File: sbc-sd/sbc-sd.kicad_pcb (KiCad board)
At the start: 4 copper layers, 55.9 x 25.4 mm, 21 parts, among them J1 SIO-Header, J2 RP2040-Zero-lhs, J3 RP2040-Zero-rhs, J4 RP2040-Zero-bottom, J5 104031-0811, U1 TXU0304, U2 LD39015M33R

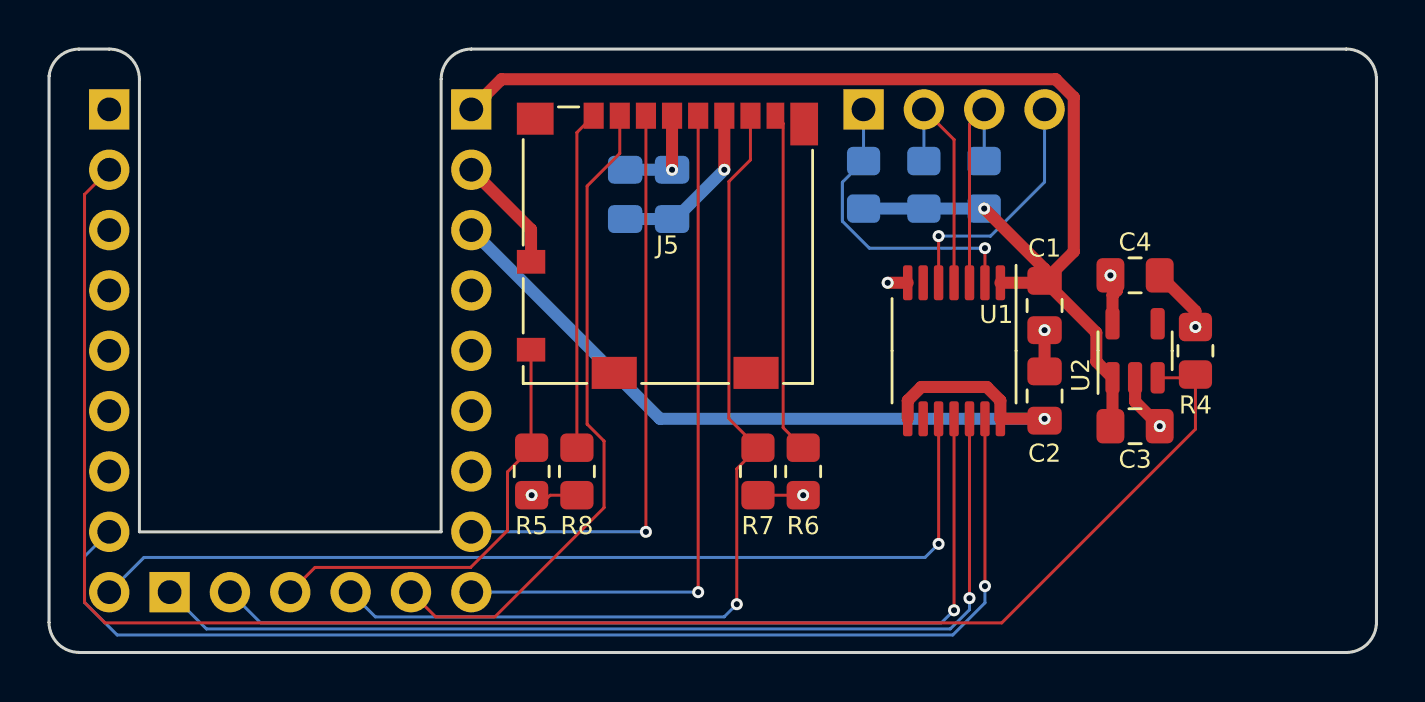
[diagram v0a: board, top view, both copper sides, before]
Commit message: SD card adapter v1.2
- Move SD card connector closer to the edge of the board
- Pullup SD detect signal to non-switched 5V
- Eliminate SD DO pullup
- Move LDO closer to SD
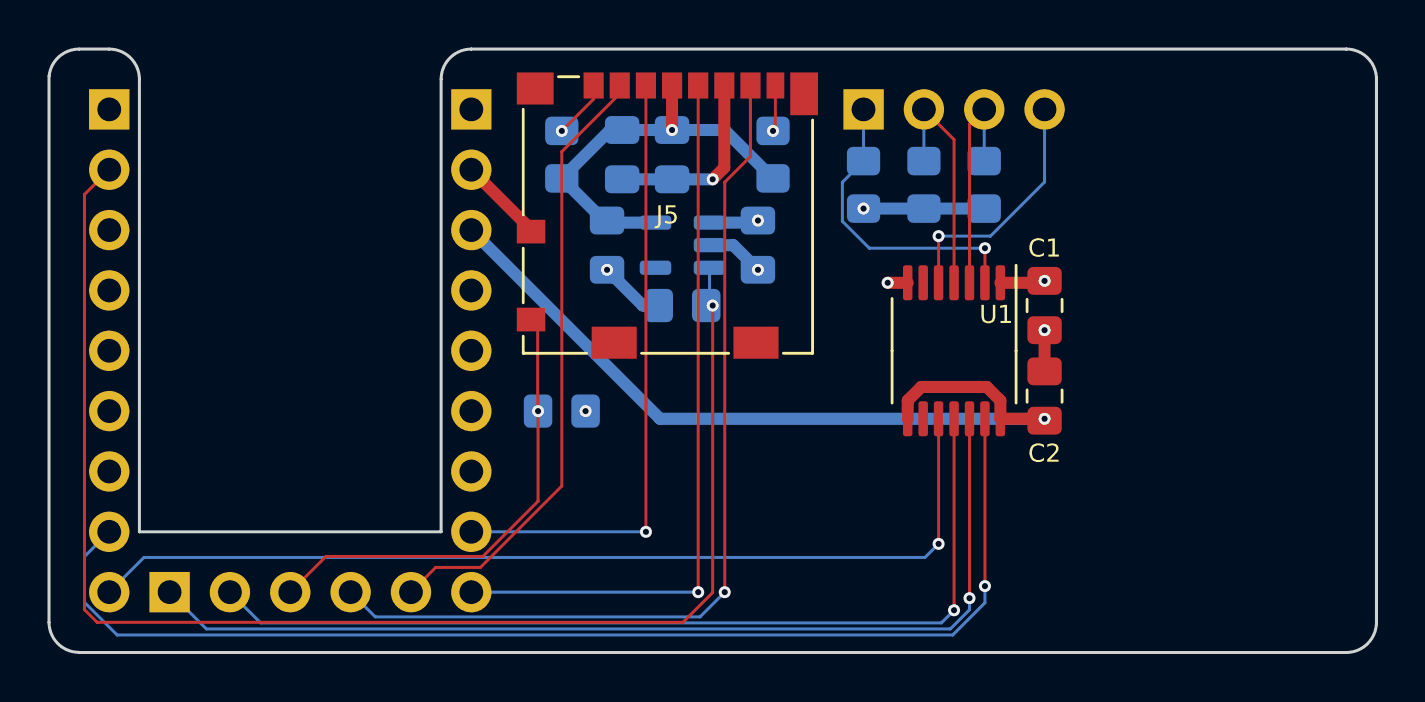
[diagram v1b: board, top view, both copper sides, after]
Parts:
- removed the R7 at (154.3, 66.0)
- C3, C4, R4, R5, R6, U2: moved to B.Cu
- R7: renamed from R8; moved to B.Cu
- moved C4 22.3 mm to (148.0, 56.5), turned to -90 degrees
- moved R4 21.7 mm to (151.1, 59.1), turned to 180 degrees
- moved U2 19.6 mm to (151.1, 56.5), turned to 180 degrees
- moved C3 17.6 mm to (154.3, 56.5), turned to -90 degrees
- moved R6 13.4 mm to (154.9, 52.7)
- moved R7 13.4 mm to (146.1, 52.7)
- moved R5 2.84 mm to (146.1, 63.5), turned to 180 degrees
- moved C6 1.68 mm to (148.6, 52.7)
- moved C5 1.67 mm to (150.7, 52.7)
- moved J5 1.27 mm to (150.5, 55.2)
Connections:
- R5 pad 1: Net-(J5-VDD) -> +5VP
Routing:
- net +5VP: track 52.6 -> 8.81 mm, vias 1 -> 4
- net SD_PWR: track 72.9 -> 59.7 mm, vias 0 -> 1
- net Net-(J5-DAT1): track 14.5 -> 1.95 mm, vias 0 -> 1
- net Net-(J5-DAT2): track 14.3 -> 2.47 mm, vias 0 -> 1
- net Net-(J5-VDD): track 10.0 -> 16.9 mm, vias 4 -> 1
- net /SD_CS: track 27.8 -> 26.1 mm
- net SD_SCLK: track 29.6 -> 30.9 mm
- net SD_DI: track 24.9 -> 26.1 mm
- net /SD_DETECT: track 18.3 -> 19.4 mm, vias 0 -> 1
- net GND: track 19.9 -> 19.4 mm
- added copper zone on In2.Cu, net +5VP
- removed copper zone on In2.Cu, net Net-(J5-VDD)
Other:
- board text added: "SFF SD v1.2 © 2023 Daniel Picken https://github.com/dpicken/atari-hw"
- board text removed: "SFF SD v1.1 © 2023 Daniel Picken https://github.com/dpicken/atari-hw"

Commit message: SBC v1.3
Motherboard updates:

  - KiCad 9 upgrade
  - USB-C power connector
  - Replace EOL resistor packs with discrete SMD resistors
  - Power/enable voltage translators from switched 5V
  - Fix motor signal pullup
  - Eliminate loop in phi2 traces
  - Thicker clock signal traces

SD card adapter updates:

  - KiCad 9 upgrade
  - Power/enable voltage translator from switched 5V and the eliminate unnecessary SIO pullups

Audio/Video adapter updates:

  - KiCad 9 upgrade
  - No functional changes, gerbers not regenerated, cleaned up bom
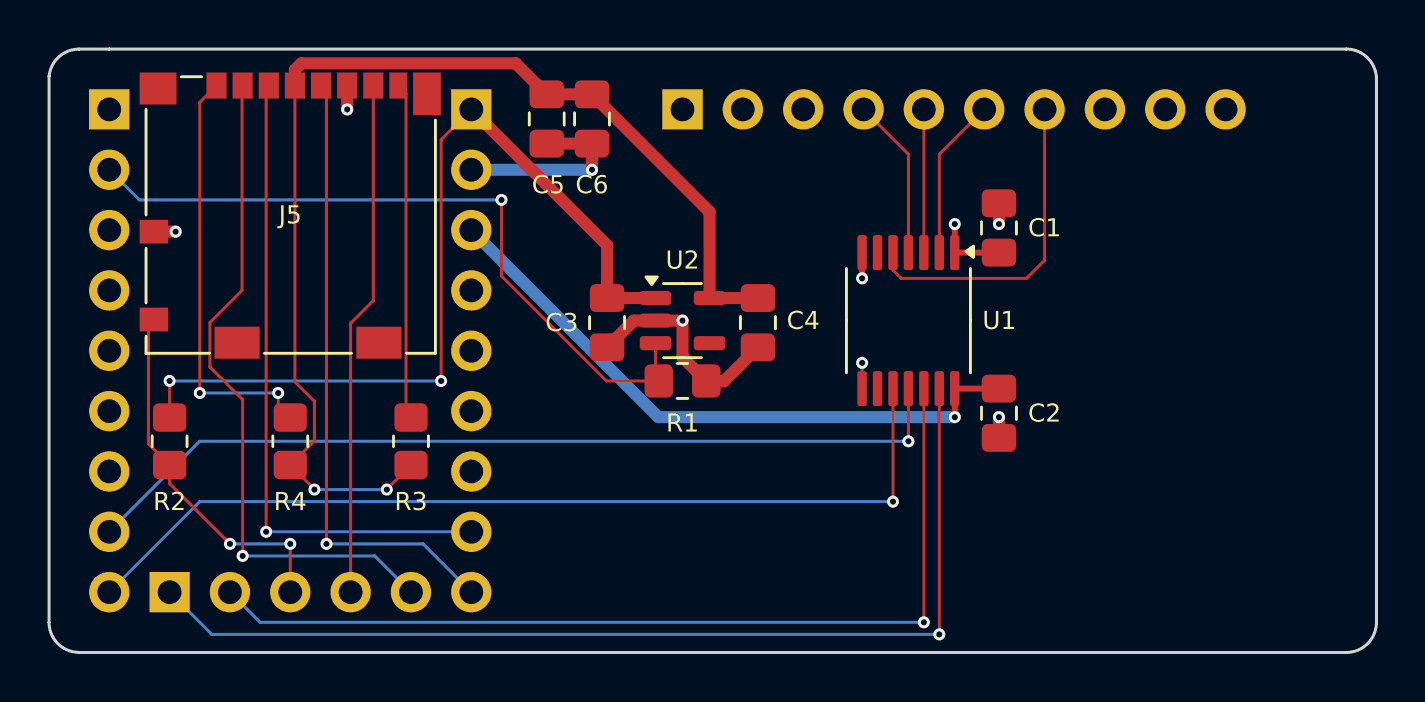
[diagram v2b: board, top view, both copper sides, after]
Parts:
- removed R5, R6, R7: 10K, Resistor_SMD:R_0805_2012Metric_Pad1.20x1.40mm_HandSolder
- C3, C4, C5, C6, R1, R2, R3, R4, U2: moved to F.Cu
- J1: footprint Connector_PinHeader_2.54mm:PinHeader_1x04_P2.54mm_Vertical -> Connector_PinHeader_2.54mm:PinHeader_1x10_P2.54mm_Vertical
- J2: value RP2040-Zero-lhs -> MC_IO-lhs
- J3: value RP2040-Zero-rhs -> MC_IO_PWR-rhs
- J4: value RP2040-Zero-bottom -> MC_IO-bottom
- moved R2 35.9 mm to (129.5, 64.8), turned to -90 degrees
- moved R3 24.1 mm to (139.7, 64.8)
- moved R4 17.5 mm to (134.6, 64.8), turned to 90 degrees
- moved J5 15.9 mm to (134.6, 55.2)
- moved R1 11.2 mm to (151.1, 62.2), turned to 0 degrees
- moved J1 7.62 mm to (151.1, 50.8)
- moved C3 7.14 mm to (148.0, 59.8)
- moved C4 7.14 mm to (154.3, 59.8)
- moved C5 5.48 mm to (145.4, 51.2)
- moved C1 3.79 mm to (164.4, 55.8), turned to 90 degrees
- moved U2 3.17 mm to (151.1, 59.7), turned to 0 degrees
- moved U1 2.30 mm to (160.6, 59.7)
- moved C2 2.05 mm to (164.4, 63.6), turned to -90 degrees
- moved C6 1.97 mm to (147.3, 51.2)
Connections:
- C1 pad 1: +5VP -> +5V
- C4 pad 1: Net-(J5-VDD) -> /SD_VDD
- C5 pad 1: Net-(J5-VDD) -> /SD_VDD
- C6 pad 1: Net-(J5-VDD) -> /SD_VDD
- J1 pad 1: SIO_MOTOR_5V -> +5V
- J1 pad 2: SIO_COMMAND_5V -> unconnected-(J1-Pin_2-Pad2)
- J1 pad 3: SIO_DATA_OUT_5V -> unconnected-(J1-Pin_3-Pad3)
- J1 pad 4: SIO_DATA_IN_5V -> SIO_MOTOR
- J5 pad 4: Net-(J5-VDD) -> /SD_VDD
- R1 pad 1: +5VP -> SD_PWR
- R1 pad 2: SIO_MOTOR_5V -> GND
- R2 pad 2: SIO_DATA_OUT_5V -> /SD_DETECT
- R3 pad 1: +5VP -> /SD_VDD
- R3 pad 2: SIO_COMMAND_5V -> Net-(J5-DAT1)
- R4 pad 1: SD_PWR -> /SD_VDD
- R4 pad 2: GND -> Net-(J5-DAT2)
- U1 pad 1: +5VP -> +5V
- U1 pad 11: SIO_COMMAND_3V3 -> SIO_MOTOR_3V3
- U1 pad 12: SIO_DATA_OUT_3V3 -> SIO_COMMAND_3V3
- U1 pad 13: SIO_MOTOR_3V3 -> SIO_DATA_OUT_3V3
- U1 pad 2: SIO_MOTOR_5V -> SIO_DATA_OUT
- U1 pad 3: SIO_DATA_OUT_5V -> SIO_COMMAND
- U1 pad 4: SIO_COMMAND_5V -> SIO_MOTOR
- U1 pad 5: SIO_DATA_IN_5V -> SIO_DATA_IN
- U1 pad 8: +3.3VP -> +5V
- U2 pad 5: Net-(J5-VDD) -> /SD_VDD
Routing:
- net /SD_VDD: track 0.00 -> 49.2 mm, vias 0 -> 2
- net SD_PWR: track 59.7 -> 30.3 mm
- net +5VP: track 8.81 -> 37.3 mm, vias 4 -> 2
- net Net-(J5-VDD): track 16.9 -> 0.00 mm, vias 1 -> 0
- net SD_DO: track 38.4 -> 21.7 mm, vias 1 -> 0
- net Net-(J5-DAT2): track 2.47 -> 17.8 mm, vias 1 -> 2
- net SIO_DATA_IN: track 0.00 -> 13.9 mm
- net SIO_MOTOR_5V: track 13.0 -> 0.00 mm, vias 1 -> 0
- net SIO_MOTOR_3V3: track 50.2 -> 37.4 mm
- net Net-(J5-DAT1): track 1.95 -> 14.2 mm, vias 1 -> 0
- net SIO_DATA_IN_5V: track 10.4 -> 0.00 mm, vias 1 -> 0
- net SIO_COMMAND_5V: track 10.00 -> 0.00 mm
- net SIO_DATA_OUT_5V: track 9.73 -> 0.00 mm
- net +3.3VP: track 35.2 -> 26.7 mm
- net SIO_DATA_OUT: track 0.00 -> 6.81 mm
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- added copper zone on In2.Cu, net +5V
- removed copper zone on In2.Cu, net +5VP
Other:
- outline, holes or cut-outs redrawn
- board text added: "SFF SD v1.3 © 2026 Daniel Picken https://github.com/dpicken/atari-hw"
- board text removed: "SFF SD v1.2 © 2023 Daniel Picken https://github.com/dpicken/atari-hw"
